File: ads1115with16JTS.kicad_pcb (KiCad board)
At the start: 2 copper layers, 127 x 152.4 mm, 41 parts, among them J1 Conn_01x02_Pin, J10 Conn_01x02_Pin, J11 Conn_01x02_Pin, J12 Conn_01x02_Pin, J13 Conn_01x02_Pin, J14 Conn_01x02_Pin, J15 Conn_01x02_Pin, J16 Conn_01x02_Pin, J17 Conn_01x04_Pin, J2 Conn_01x02_Pin, J3 Conn_01x02_Pin, J4 Conn_01x02_Pin, J5 Conn_01x02_Pin, J6 Conn_01x02_Pin, J7 Conn_01x02_Pin, J8 Conn_01x02_Pin, J9 Conn_01x02_Pin, U1 ADS1115IDGS, U2 ADS1115IDGS, U3 ADS1115IDGS, U4 ADS1115IDGS

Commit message: snapshot v0.0.10
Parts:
- added J18: PinSocket_1x20_P2.54mm_Vertical, PG:b_pill_socket_1-20, F.Cu at (78.0, 64.8)
- added J18b1: SolderWire-0.25sqmm_1x20_P4.2mm_D0.65mm_OD1.7mm, PG:b_pill_takeoffPads_1-20, F.Cu at (86.1, 64.8)
- added J19: PinSocket_1x20_P2.54mm_Vertical, PG:b_pill_socket_21-40, F.Cu at (93.2, 64.8)
- added J19b1: SolderWire-0.25sqmm_1x20_P4.2mm_D0.65mm_OD1.7mm, PG:b_pill_takeoffPads_21-40, F.Cu at (90.2, 64.8)
- added pads1: SolderWire-0.25sqmm_1x04_P4.2mm_D0.65mm_OD1.7mm, Connector_Wire:SolderWire-0.25sqmm_1x04_P4.2mm_D0.65mm_OD1.7mm, F.Cu at (80.0, 27.9)
- J1, J10, J11, J12, J13, J14, J15, J16, J2, J3, J4, J5, J6, J7, J8, J9: footprint Connector_JST:JST_XH_S2B-XH-A_1x02_P2.50mm_Horizontal -> Connector_JST:JST_XH_B2B-XH-A_1x02_P2.50mm_Vertical
- R1, R10, R11, R12, R13, R14, R15, R16, R2, R3, R4, R5, R6, R7, R8, R9: footprint Resistor_SMD:R_0805_2012Metric -> Resistor_SMD:R_0603_1608Metric
- moved J16 78.0 mm to (64.9, 88.4), turned to 0 degrees
- moved R16 76.9 mm to (61.0, 91.4)
- moved 0.1µF4 73.1 mm to (72.4, 88.4)
- moved U4 72.7 mm to (72.4, 82.0)
- moved R15 72.2 mm to (61.0, 87.2)
- moved J15 69.6 mm to (54.7, 88.4), turned to 0 degrees
- moved J14 67.3 mm to (64.9, 81.3), turned to 0 degrees
- moved R14 66.9 mm to (61.0, 83.7)
- moved R13 62.2 mm to (61.0, 79.6)
- moved J12 59.6 mm to (64.9, 71.3), turned to 0 degrees
- moved J13 59.0 mm to (54.7, 81.2), turned to 0 degrees
- moved R12 58.7 mm to (61.0, 74.3)
- moved U3 55.1 mm to (72.4, 64.9)
- moved 0.1µF3 54.7 mm to (72.4, 71.3)
- moved R11 54.0 mm to (61.0, 70.1)
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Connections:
- net Net-(J17-Pin_3) renamed /SDA1
- net Net-(J17-Pin_4) renamed /SCL1
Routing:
- net GND: track 574.0 -> 222.8 mm, vias 9 -> 0
- net /SCL1: track 136.3 -> 109.3 mm
- net /SDA1: track 136.2 -> 115.3 mm
- net Net-(J8-Pin_1): track 25.9 -> 14.7 mm
- net Net-(J16-Pin_1): track 24.5 -> 14.7 mm
- net Net-(J12-Pin_1): track 23.1 -> 14.7 mm
- net +3V3: track 232.1 -> 240.5 mm, vias 13 -> 18
- net Net-(J1-Pin_1): track 25.5 -> 19.2 mm
- net Net-(J2-Pin_1): track 17.9 -> 12.4 mm
- net Net-(J9-Pin_1): track 24.2 -> 19.2 mm
- net Net-(J18-G): track 0.00 -> 4.45 mm
- net Net-(J18-5v): track 0.00 -> 4.45 mm
- net Net-(J18-3v3): track 0.00 -> 4.45 mm
- net Net-(J11-Pin_1): track 14.2 -> 18.5 mm
- net Net-(J13-Pin_1): track 23.4 -> 19.2 mm
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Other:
- board size 127 x 152.4 mm -> 45.7 x 68.6 mm

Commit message: changes for v0.0.12
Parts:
- removed J18b1: SolderWire-0.25sqmm_1x20_P4.2mm_D0.65mm_OD1.7mm, PG:b_pill_takeoffPads_1-20
- removed J19b1: SolderWire-0.25sqmm_1x20_P4.2mm_D0.65mm_OD1.7mm, PG:b_pill_takeoffPads_21-40
- added J**1: SolderWire-0.25sqmm_1x20_P4.2mm_D0.65mm_OD1.7mm, PG:b_pill_takeoffPads_1-20, F.Cu at (86.2, 64.6)
- added J**2: SolderWire-0.25sqmm_1x20_P4.2mm_D0.65mm_OD1.7mm, PG:b_pill_takeoffPads_21-40, F.Cu at (89.9, 64.8)
- added Mount1: MountingHole_2.2mm_M2_ISO7380_Pad, MountingHole:MountingHole_2.2mm_M2_ISO7380_Pad, F.Cu at (76.2, 27.8)
- added Mount2: MountingHole_2.2mm_M2_ISO7380_Pad, MountingHole:MountingHole_2.2mm_M2_ISO7380_Pad, F.Cu at (86.0, 91.3)
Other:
- board text added: "v0.1.0 2023-07"

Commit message: v0.0.14 snapshot.
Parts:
- removed Mount1, Mount2: MountingHole_2.2mm_M2_ISO7380_Pad, MountingHole:MountingHole_2.2mm_M2_ISO7380_Pad
- added H1: MountingHole, MountingHole:MountingHole_2.2mm_M2_ISO7380_Pad, F.Cu at (86.1, 91.6)
- added H2: MountingHole, MountingHole:MountingHole_2.2mm_M2_ISO7380_Pad, F.Cu at (77.5, 28.2)
- moved pads1 15.4 mm to (93.2, 35.8), turned to 180 degrees
- moved J17 7.17 mm to (90.4, 30.1), turned to 180 degrees
- moved R16 0.94 mm to (61.0, 90.4)
- moved R8 0.94 mm to (61.0, 56.1)
- moved R4 0.89 mm to (61.0, 39.2)
- moved R12 0.61 mm to (61.1, 73.7)
- moved R11 0.23 mm to (61.1, 70.4)
- moved R1 0.19 mm to (61.0, 28.6)
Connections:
- J**1 pad 19: Net-(J18-G) -> GND
- J18 pad 19: Net-(J18-G) -> GND
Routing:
- net +3V3: track 240.5 -> 300.6 mm, vias 18 -> 0
- net GND: track 222.8 -> 177.0 mm, vias 0 -> 5
- net /SDA1: track 115.3 -> 95.4 mm
- net /SCL1: track 109.3 -> 93.5 mm
- net Net-(J18-G): track 4.45 -> 0.00 mm
- net Net-(J19-5v): track 3.81 -> 4.57 mm

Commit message: snapshot v0.1.0-pre
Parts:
- removed pads1: SolderWire-0.25sqmm_1x04_P4.2mm_D0.65mm_OD1.7mm, Connector_Wire:SolderWire-0.25sqmm_1x04_P4.2mm_D0.65mm_OD1.7mm
- added J20: TerminalBlock_Phoenix_MPT-0,5-2-2.54_1x02_P2.54mm_Horizontal, TerminalBlock_Phoenix:TerminalBlock_Phoenix_MPT-0,5-2-2.54_1x02_P2.54mm_Horizontal, F.Cu at (91.6, 36.8)
- moved J17 0.92 mm to (90.9, 29.3)
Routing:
- net /SCL1: track 93.5 -> 123.2 mm
- net /SDA1: track 95.4 -> 116.3 mm
- net GND: track 177.0 -> 171.4 mm
- net +3V3: track 300.6 -> 305.1 mm
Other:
- board text added: "v0.1.0 2023-08"
- board text removed: "v0.1.0 2023-07"

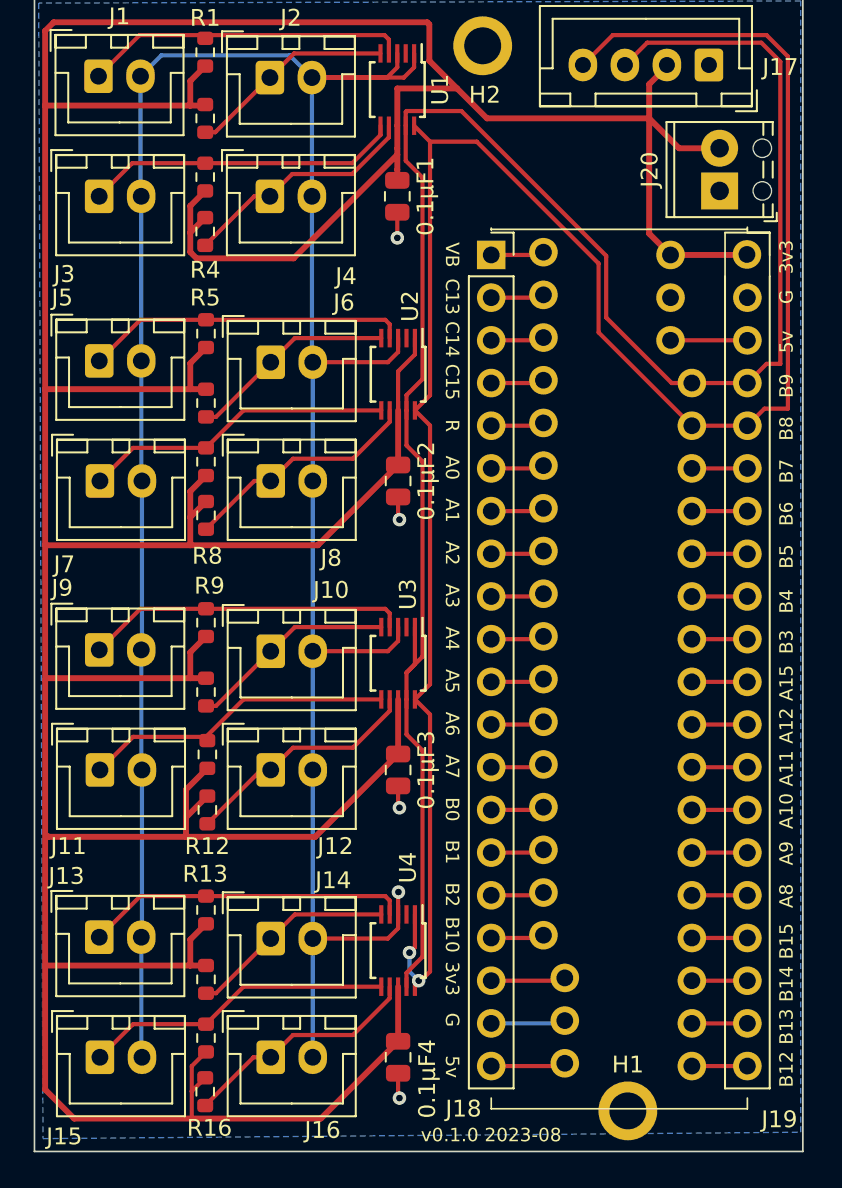
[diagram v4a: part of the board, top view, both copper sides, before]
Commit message: change solder mask for takeoff pads, which will not be soldered.
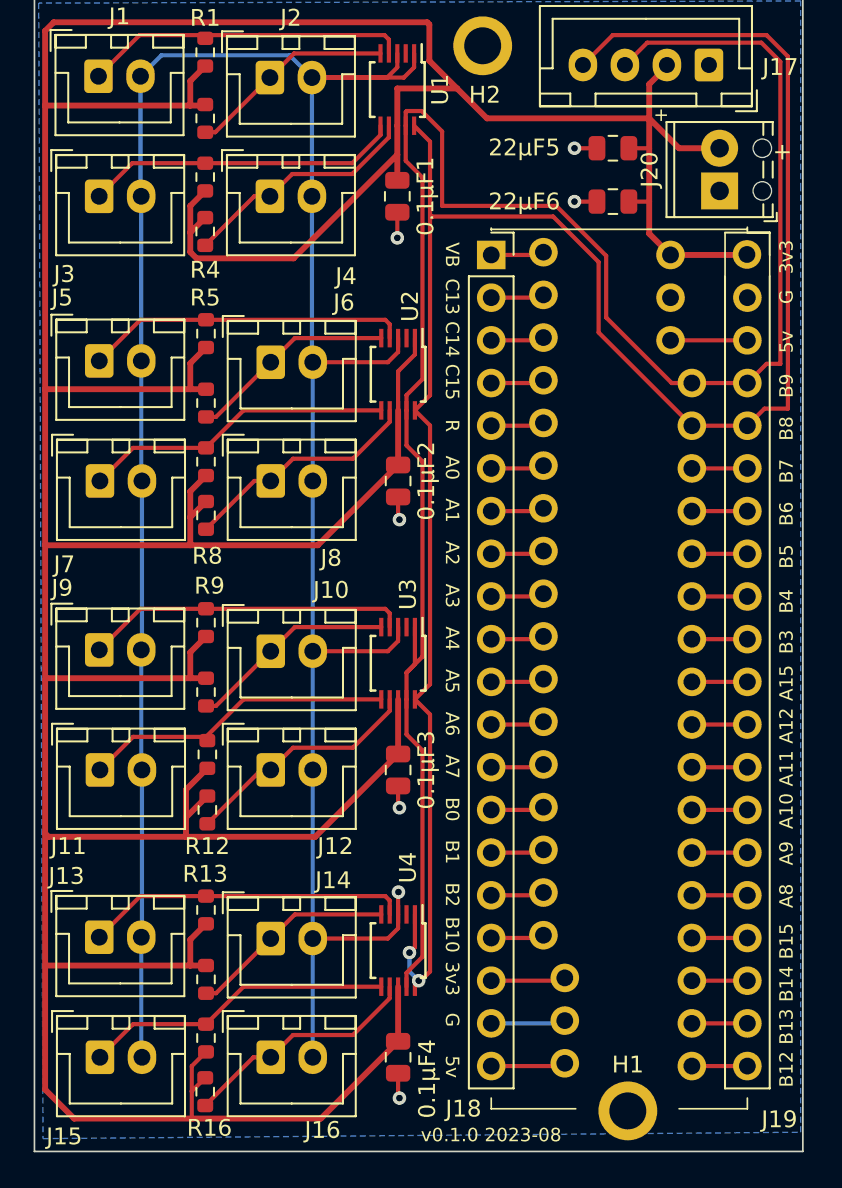
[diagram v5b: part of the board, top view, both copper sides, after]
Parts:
- added 22µF5: C5, Capacitor_SMD:C_0805_2012Metric, F.Cu at (85.2, 34.3)
- added 22µF6: C6, Capacitor_SMD:C_0805_2012Metric, F.Cu at (85.2, 37.5)
- 0.1µF1: value C -> C1
- 0.1µF2: value C -> C2
- 0.1µF3: value C -> C3
- 0.1µF4: value C -> C4
- J20: value TerminalBlock_Phoenix_MPT-0,5-2-2.54_1x02_P2.54mm_Horizontal -> Screw_Terminal_01x02
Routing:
- net GND: track 171.4 -> 174.0 mm, vias 5 -> 7
- net +3V3: track 305.1 -> 307.7 mm
- net /SDA1: track 116.3 -> 118.9 mm
- net /SCL1: track 123.2 -> 121.5 mm
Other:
- board text added: "+"

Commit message: adjustments to mask and silkscreen.
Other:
- board text added: "SCL1"
- board text added: "SDA1"
- board text added: "ads1115with16JTS"
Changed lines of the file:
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@@
         (effects (font (size 1 1) (thickness 0.15)))
     )
-    (fp_text value "Conn_01x02_Pin" (at 1.25 4.6) (layer "F.Fab")
+    (fp_text value "Conn_01x02_Pin" (at 1.4365 0.3955) (layer "F.Fab")
         (effects (font (size 1 1) (thickness 0.15)))
     )
@@
         (effects (font (size 1 1) (thickness 0.15)))
     )
-    (fp_text value "Conn_01x02_Pin" (at 1.25 4.6) (layer "F.Fab")
+    (fp_text value "Conn_01x02_Pin" (at -2.45 0.525) (layer "F.Fab")
         (effects (font (size 1 1) (thickness 0.15)))
     )
@@
         (effects (font (size 1 1) (thickness 0.15)))
     )
-    (fp_text value "Conn_01x02_Pin" (at 1.25 4.6) (layer "F.Fab")
+    (fp_text value "Conn_01x02_Pin" (at -2.45 0.525) (layer "F.Fab")
         (effects (font (size 1 1) (thickness 0.15)))
     )
@@
         (effects (font (size 1 1) (thickness 0.15)))
     )
-    (fp_text value "Conn_01x02_Pin" (at 1.25 4.6) (layer "F.Fab")
+    (fp_text value "Conn_01x02_Pin" (at 1.5635 0.4755) (layer "F.Fab")
         (effects (font (size 1 1) (thickness 0.15)))
     )
@@
         (effects (font (size 1 1) (thickness 0.15)))
     )
-    (fp_text value "Conn_01x02_Pin" (at 1.25 4.6) (layer "F.Fab")
+    (fp_text value "Conn_01x02_Pin" (at 1.484 0.315) (layer "F.Fab")
         (effects (font (size 1 1) (thickness 0.15)))
     )
@@
         (effects (font (size 1 1) (thickness 0.15)))
     )
-    (fp_text value "ADS1115IDGS" (at 0 2.55 -90) (layer "F.Fab")
+    (fp_text value "ADS1115IDGS" (at -1 -1 -90) (layer "F.Fab")
         (effects (font (size 1 1) (thickness 0.15)))
     )
@@
         (effects (font (size 1 1) (thickness 0.15)))
     )
-    (fp_text value "ADS1115IDGS" (at 0 2.55 -90) (layer "F.Fab")
+    (fp_text value "ADS1115IDGS" (at -1 -1 -90) (layer "F.Fab")
         (effects (font (size 1 1) (thickness 0.15)))
     )
@@
         (effects (font (size 1 1) (thickness 0.15)))
     )
-    (fp_text value "Conn_01x02_Pin" (at 1.25 4.6) (layer "F.Fab")
+    (fp_text value "Conn_01x02_Pin" (at -2.45 0.525) (layer "F.Fab")
         (effects (font (size 1 1) (thickness 0.15)))
     )
@@
         (effects (font (size 1 1) (thickness 0.15)))
     )
-    (fp_text value "Conn_01x02_Pin" (at 1.25 4.6) (layer "F.Fab")
+    (fp_text value "Conn_01x02_Pin" (at 1.5635 0.5225) (layer "F.Fab")
         (effects (font (size 1 1) (thickness 0.15)))
     )
@@
         (effects (font (size 1 1) (thickness 0.1)))
     )
-    (fp_text value "SolderWire-0.25sqmm_1x20_P4.2mm_D0.65mm_OD1.7mm" (at 0.254 2.794 90 unlocked) (layer "F.Fab")
+    (fp_text value "SolderWire-0.25sqmm_1x20_P4.2mm_D0.65mm_OD1.7mm" (at -0.127 -3.302 90 unlocked) (layer "F.Fab")
         (effects (font (size 1 1) (thickness 0.15)))
     )
@@
         (effects (font (size 1 1) (thickness 0.15)))
     )
-    (fp_text value "Conn_01x02_Pin" (at 1.25 4.6) (layer "F.Fab")
+    (fp_text value "Conn_01x02_Pin" (at 1.865 0.649) (layer "F.Fab")
         (effects (font (size 1 1) (thickness 0.15)))
     )
@@
         (effects (font (size 1 1) (thickness 0.1)))
     )
-    (fp_text value "PinSocket_1x20_P2.54mm_Vertical" (at 5.08 0 90 unlocked) (layer "F.Fab")
+    (fp_text value "PinSocket_1x20_P2.54mm_Vertical" (at 0.127 5.207 90 unlocked) (layer "F.Fab")
         (effects (font (size 1 1) (thickness 0.15)))
     )
@@
         (effects (font (size 1 1) (thickness 0.15)))
     )
-    (fp_text value "ADS1115IDGS" (at 0 2.55 -90) (layer "F.Fab")
+    (fp_text value "ADS1115IDGS" (at -1 -1 -90) (layer "F.Fab")
         (effects (font (size 1 1) (thickness 0.15)))
     )
@@
         (effects (font (size 1 1) (thickness 0.15)))
     )
-    (fp_text value "Conn_01x04_Pin" (at 3.556 4.826) (layer "F.Fab")
+    (fp_text value "Conn_01x04_Pin" (at 3.556 0.635) (layer "F.Fab")
         (effects (font (size 1 1) (thickness 0.15)))
     )
@@
         (effects (font (size 1 1) (thickness 0.15)))
     )
-    (fp_text value "ADS1115IDGS" (at 0 2.55 -90) (layer "F.Fab")
+    (fp_text value "ADS1115IDGS" (at -1 -1 -90) (layer "F.Fab")
         (effects (font (size 1 1) (thickness 0.15)))
     )
@@
         (effects (font (size 1 1) (thickness 0.15)))
     )
-    (fp_text value "Conn_01x02_Pin" (at 1.25 4.6) (layer "F.Fab")
+    (fp_text value "Conn_01x02_Pin" (at 2.0715 -0.0325) (layer "F.Fab")
         (effects (font (size 1 1) (thickness 0.15)))
     )
@@
         (effects (font (size 1 1) (thickness 0.15)))
     )
-    (fp_text value "Conn_01x02_Pin" (at 1.25 4.6) (layer "F.Fab")
+    (fp_text value "Conn_01x02_Pin" (at -2.45 0.525) (layer "F.Fab")
         (effects (font (size 1 1) (thickness 0.15)))
     )
@@
         (effects (font (size 1 1) (thickness 0.15)))
     )
-    (fp_text value "Conn_01x02_Pin" (at 1.25 4.6) (layer "F.Fab")
+    (fp_text value "Conn_01x02_Pin" (at -2.45 0.525) (layer "F.Fab")
         (effects (font (size 1 1) (thickness 0.15)))
     )
@@
         (effects (font (size 1 1) (thickness 0.15)))
     )
-    (fp_text value "Conn_01x02_Pin" (at 1.25 4.6) (layer "F.Fab")
+    (fp_text value "Conn_01x02_Pin" (at 1.6905 0.8535) (layer "F.Fab")
         (effects (font (size 1 1) (thickness 0.15)))
     )
@@
         (effects (font (size 1 1) (thickness 0.1)))
     )
-    (fp_text value "SolderWire-0.25sqmm_1x20_P4.2mm_D0.65mm_OD1.7mm" (at -4.504 3.34 90 unlocked) (layer "F.Fab")
+    (fp_text value "SolderWire-0.25sqmm_1x20_P4.2mm_D0.65mm_OD1.7mm" (at -5.139 -3.772 90 unlocked) (layer "F.Fab")
         (effects (font (size 1 1) (thickness 0.15)))
     )
@@
         (effects (font (size 1 1) (thickness 0.15)))
     )
-    (fp_text value "Conn_01x02_Pin" (at 1.25 4.6) (layer "F.Fab")
+    (fp_text value "Conn_01x02_Pin" (at -2.45 0.525) (layer "F.Fab")
         (effects (font (size 1 1) (thickness 0.15)))
     )
@@
         (effects (font (size 1 1) (thickness 0.15)))
     )
-    (fp_text value "Screw_Terminal_01x02" (at 0.762 29.083) (layer "F.Fab")
+    (fp_text value "Screw_Terminal_01x02" (at 1.016 12.192) (layer "F.Fab")
         (effects (font (size 1 1) (thickness 0.15)))
     )
@@
         (effects (font (size 1 1) (thickness 0.15)))
     )
-    (fp_text value "Conn_01x02_Pin" (at 1.25 4.6) (layer "F.Fab")
+    (fp_text value "Conn_01x02_Pin" (at -2.45 0.525) (layer "F.Fab")
         (effects (font (size 1 1) (thickness 0.15)))
     )
@@
         (effects (font (size 1 1) (thickness 0.15)))
     )
-    (fp_text value "Conn_01x02_Pin" (at 1.25 4.6) (layer "F.Fab")
+    (fp_text value "Conn_01x02_Pin" (at 1.6905 0.5525) (layer "F.Fab")
         (effects (font (size 1 1) (thickness 0.15)))
     )
@@
         (effects (font (size 1 1) (thickness 0.15)))
     )
-    (fp_text value "Conn_01x02_Pin" (at 1.25 4.6) (layer "F.Fab")
+    (fp_text value "Conn_01x02_Pin" (at -2.45 0.525) (layer "F.Fab")
         (effects (font (size 1 1) (thickness 0.15)))
     )
@@
   (gr_rect (start 50.8 25.4) (end 96.52 93.98)
     (stroke (width 0.1) (type default)) (fill none) (layer "Edge.Cuts"))
+  (gr_text "SCL1" (at 85.852 51.308) (layer "F.SilkS")
+    (effects (font (size 0.8 0.8) (thickness 0.15)) (justify left bottom))
+  )
   (gr_text "v0.1.0 2023-08" (at 73.787 93.472) (layer "F.SilkS")
     (effects (font (size 0.8 0.8) (thickness 0.1)) (justify left bottom))
   )
+  (gr_text "ads1115with16JTS" (at 86.614 86.614 90) (layer "F.SilkS")
+    (effects (font (size 1 1) (thickness 0.15)) (justify left bottom))
+  )
   (gr_text "+" (at 87.63 32.766) (layer "F.SilkS")
     (effects (font (size 0.8 0.8) (thickness 0.15)) (justify left bottom))
@@
     (effects (font (size 1 1) (thickness 0.15)) (justify left bottom))
   )
+  (gr_text "SDA1" (at 85.852 48.768) (layer "F.SilkS")
+    (effects (font (size 0.8 0.8) (thickness 0.15)) (justify left bottom))
+  )
   (segment (start 51.943 26.797) (end 74.168 26.797) (width 0.35) (layer "F.Cu") (net 1))

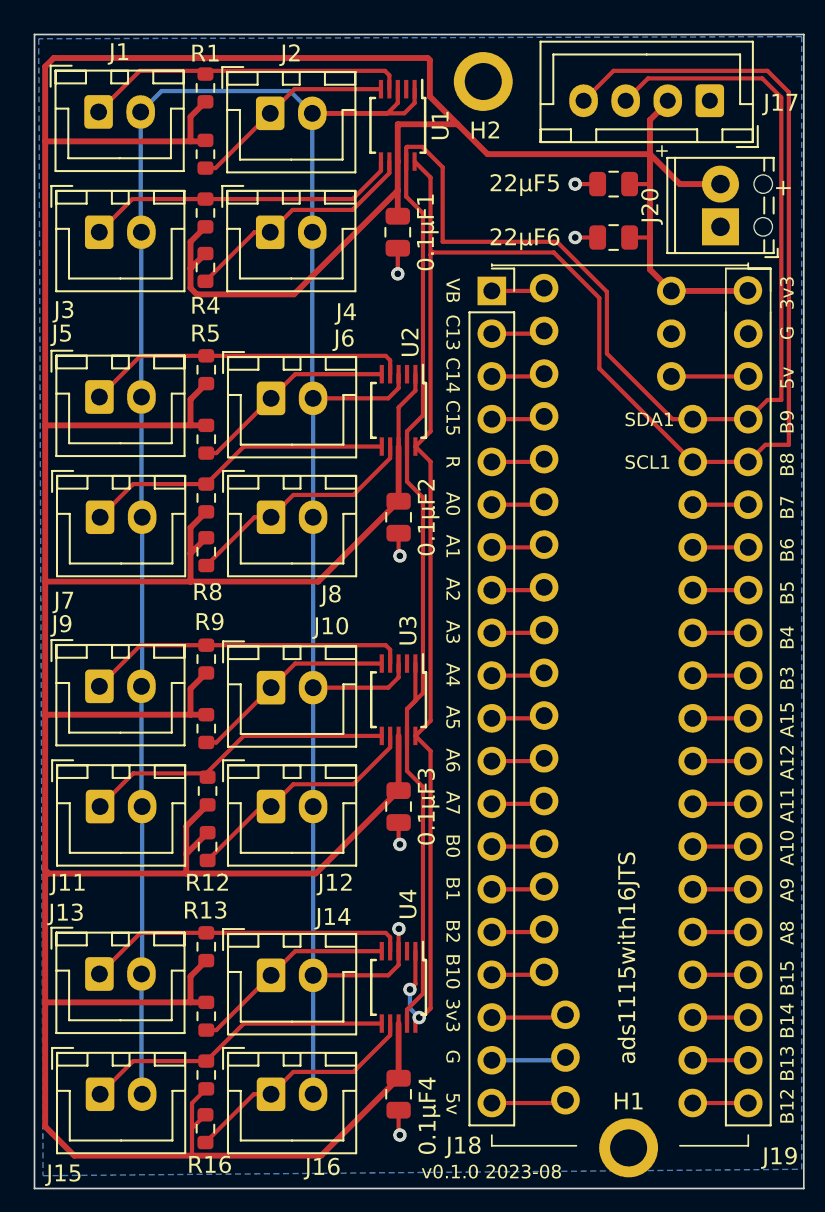
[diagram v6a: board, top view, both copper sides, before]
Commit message: moved PG.kicad_sym to ProjectLib.kicad_sym and added all project symbols so project has a complete set of stable symbols.
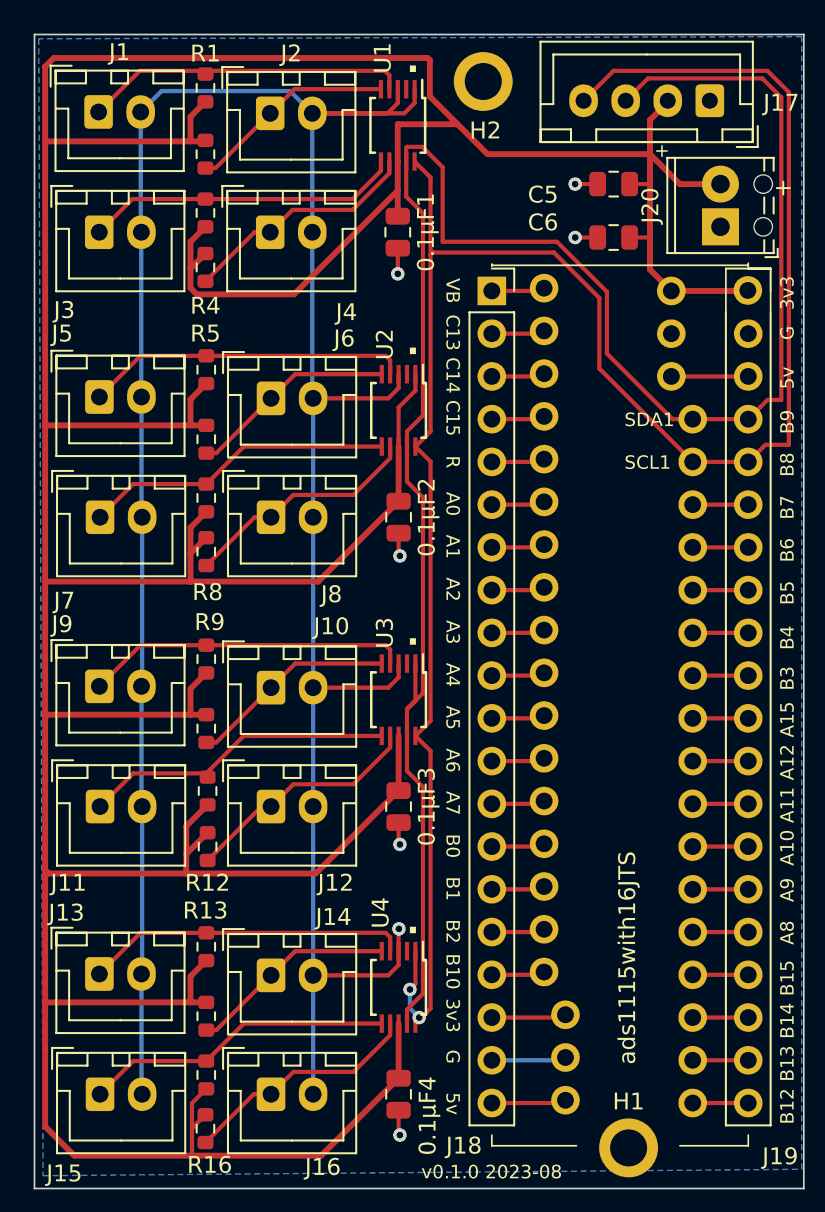
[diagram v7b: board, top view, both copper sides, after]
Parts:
- C5: renamed from 22µF5; value C5 -> 22µF5
- C6: renamed from 22µF6; value C6 -> 22µF6
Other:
- board text added: "."
